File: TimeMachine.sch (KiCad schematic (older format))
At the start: 52 parts, among them J1 AppleIIBus, J2 JTAG, U1 EPM7128SL84, U2 DS1215, U3 74AHCT04, U4 AS6C8008, U5 39F040, Y1 32k768

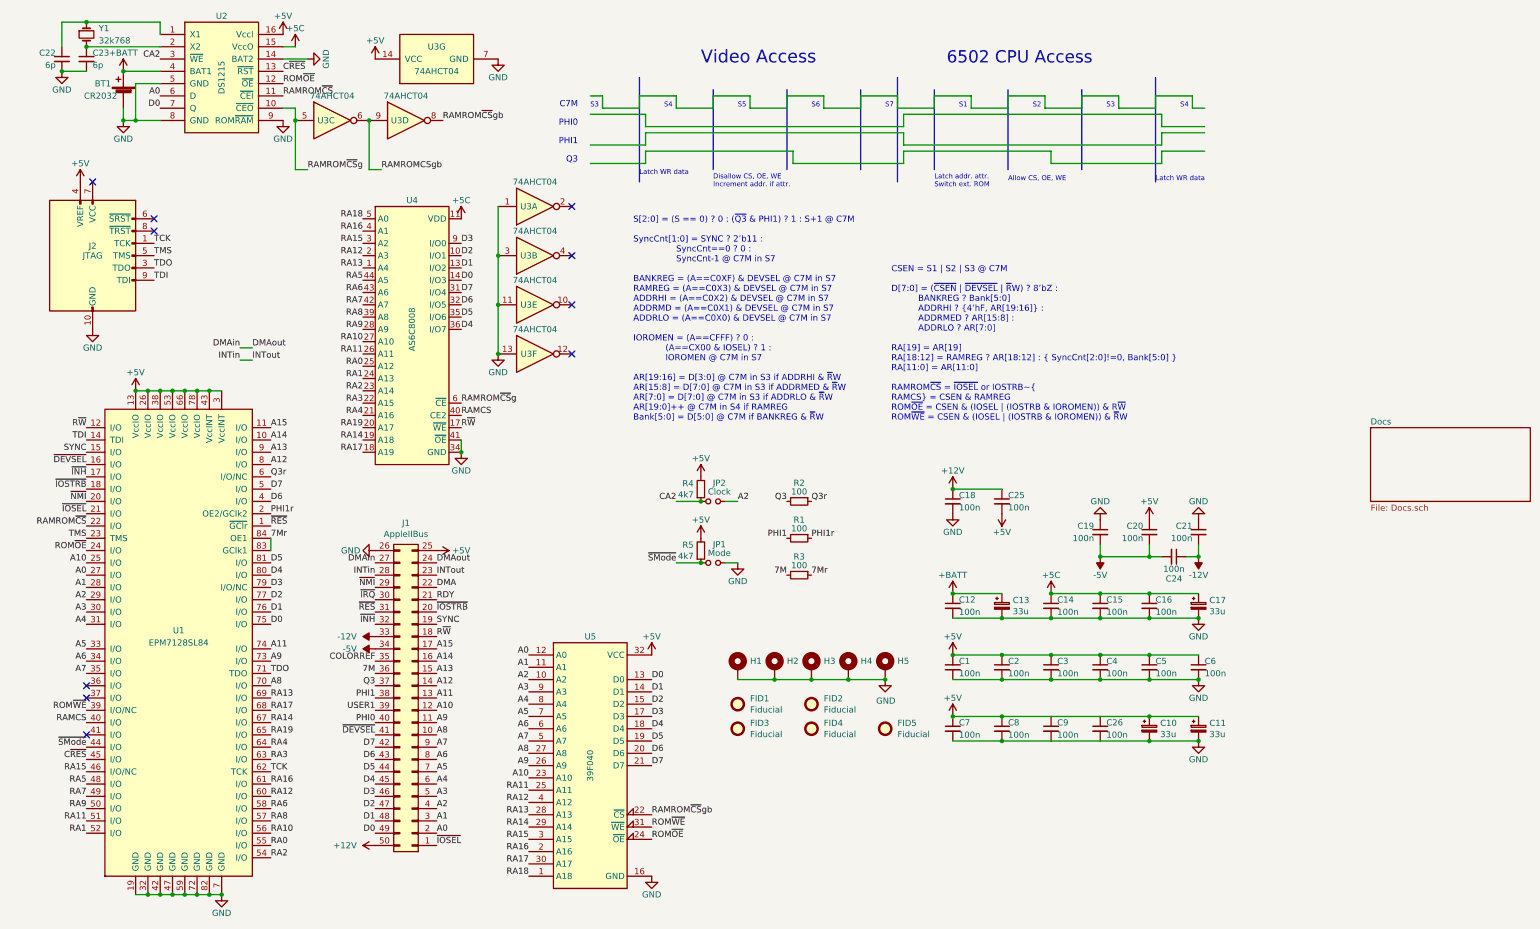
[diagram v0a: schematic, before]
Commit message: Buffered data bus with CPLD
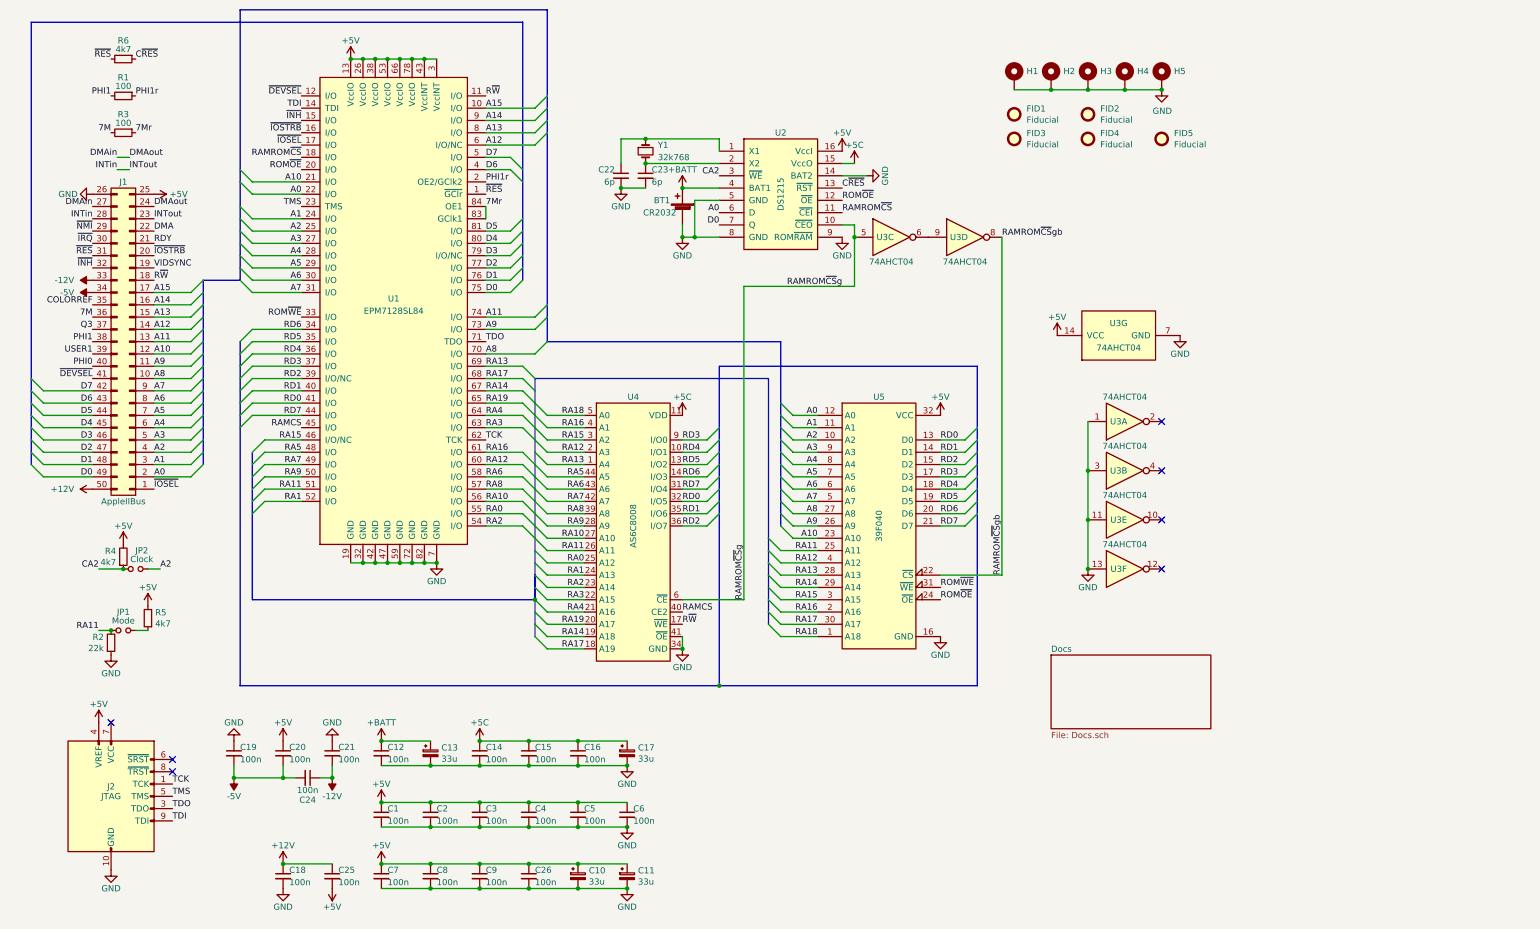
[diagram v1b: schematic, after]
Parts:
- added R6: 4k7, stdpads:R_0805, symbol Device:R_Small
- R2: value 100 -> 22k
- U3: footprint Package_SO:SOIC-14_3.9x8.7mm_P1.27mm -> stdpads:SOIC-14_3.9mm
- U3: footprint 74AHCT04 -> stdpads:SOIC-14_3.9mm
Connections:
- net labels added: RD0, RD1, RD2, RD3, RD4, RD5, RD6, RD7, VIDSYNC
- net labels removed: Q3r, RAMROMCSgb, SYNC, ~SMode~
- wire segments 145 -> 217
- no-connect marks 10 -> 7
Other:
- note removed: "6502 CPU Access"
- note removed: "Allow CS, OE, WE"
- note removed: "C7M"
- note removed: "CSEN = S1 | S2 | S3 @ C7M\n\nD[7:0] = (~CSEN~ | ~DEVSEL~ | ~R~W) ? 8’bZ :\n BANKREG ? Bank[5:0]\n ADDRHI ? {4’hF, AR[19:16]} : \n ADDRMED ? AR[15:8] : \n ADDRLO ? AR[7:0]\n\nRA[19] = AR[19]\nRA[18:12] = RAMREG ? AR[18:12] : { SyncCnt[2:0]!=0, Bank[5:0] }\nRA[11:0] = AR[11:0]\n\nRAMROM~CS~ = ~IOSEL or IOSTRB~\nRAMCS = CSEN & RAMREG\nROM~OE~ = CSEN & (IOSEL | (IOSTRB & IOROMEN)) & R~W~\nROM~WE~ = C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"
- note removed: "Disallow CS, OE, WE\nIncrement addr. if attr."
- note removed: "Latch WR data"
- note removed: "Latch addr. attr.\nSwitch ext. ROM"
- note removed: "PHI0"
- note removed: "PHI1"
- note removed: "Q3"
- note removed: "S1"
- note removed: "S2"
- note removed: "S3"
- note removed: "S4"
- note removed: "S5"
- note removed: "S6"
- note removed: "S7"
- note removed: "S[2:0] = (S == 0) ? 0 : (~Q3~ & PHI1) ? 1 : S+1 @ C7M\n\nSyncCnt[1:0] = SYNC ? 2’b11 : \n SyncCnt==0 ? 0 :\n SyncCnt-1 @ C7M in S7\n\nBANKREG = (A==C0XF) & DEVSEL @ C7M in S7\nRAMREG = (A==C0X3) & DEVSEL @ C7M in S7\nADDRHI = (A==C0X2) & DEVSEL @ C7M in S7\nADDRMD = (A==C0X1) & DEVSEL @ C7M in S7\nADDRLO = (A==C0X0) & DEVSEL @ C7M in S7\n\nIOROMEN = (A==CFFF) ? 0 :\n (A==CX00 & IOSEL) ? 1 :\n IOR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"
- note removed: "Video Access"
- moved on the sheet: BT1, C1, C10, C11, C12, C13, C14, C15, C16, C17, C18, C19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

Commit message: Changed ROM OE strategy
Has gerbers submitted to JLCPCB though
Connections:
- net GND: now also U3.9; no longer U3.3
- net RAMROM~CS~: now also U1.20 (I/O); no longer U1.18 (I/O)
- net R~W~: now also U3.3, U5.31 (~WE~)
- net ~IOSEL~: now also U1.18 (I/O); no longer U1.17 (I/O)
- net ~OE~: now reaches U3.4
- net ~OE~: now also U2.12 (~OE~), U5.24 (~OE~)
- net RAMROMCSgb: now reaches U3.6
- net RAMROMCSgb: now also U1.33 (I/O); no longer U3.9
- net RAMROM~CS~gb: no longer names the net of U3.8
- net RAMROM~CS~gb: no longer U5.22 (~CS~)
- removed net ROM~OE~: U1.20 (I/O), U2.12 (~OE~), U5.24 (~OE~)
- removed net ROM~WE~: U1.33 (I/O), U5.31 (~WE~)
- new net ROM~CS~: U1.17 (I/O), U5.22 (~CS~)
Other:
- moved on the sheet: U3A, U3B, U3E, U3F, U3G
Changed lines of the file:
@@
 Wire Wire Line
 	4300 2300 4300 2200
-Text Label 2800 1800 2    50   ~ 0
+Text Label 2800 1900 2    50   ~ 0
 RAMROM~CS~
-Text Label 2800 3100 2    50   ~ 0
-ROM~WE~
 Wire Wire Line
 	3200 5100 3300 5100
@@
 Text Label 2800 1500 2    50   ~ 0
 ~INH~
-Text Label 2800 1700 2    50   ~ 0
+Text Label 2800 1800 2    50   ~ 0
 ~IOSEL~
 Text Label 4300 1300 0    50   ~ 0
@@
 $EndComp
 Text Label 8500 2450 0    50   ~ 0
-RAMROM~CS~gb
+RAMROMCSgb
 Text Label 4300 2800 0    50   ~ 0
 D1
@@
 ~IOSEL~
 Text Label 8000 5400 0    50   ~ 0
-ROM~OE~
-Text Label 2800 1900 2    50   ~ 0
-ROM~OE~
+~OE~
 $Comp
 L Device:C_Small C21
@@
 	1    0    0    -1
 $EndComp
-Text Label 8000 5300 0    50   ~ 0
-ROM~WE~
 Text Label 4300 1400 0    50   ~ 0
 A15
@@
 	6400 5400 6400 2850
 Wire Wire Line
-	8500 2450 8500 5200
-Wire Wire Line
 	7300 2450 7300 2850
 Text Label 7200 2850 2    50   ~ 0
@@
 Text Label 7200 2050 0    50   ~ 0
 C~RES~
-$Comp
-L 74xx:74HC04 U3
-U 4 1 5E7FE38F
-P 8200 2450
-F 0 "U3" H 8150 2450 50  0000 C CNN
-F 1 "74AHCT04" H 8200 2250 50  0000 C CNN
-F 2 "stdpads:SOIC-14_3.9mm" H 8200 2450 50  0001 C CNN
-F 3 "https://assets.nexperia.com/documents/data-sheet/74HC_HCT04.pdf" H 8200 2450 50  0001 C CNN
-	4    8200 2450
-	1    0    0    -1
-$EndComp
-Text Label 7200 2150 0    50   ~ 0
-ROM~OE~
 $Comp
 L power:GND #PWR0123
@@
 Wire Wire Line
 	5900 5400 6400 5400
-Wire Wire Line
-	8000 5200 8500 5200
-Text Label 8500 5200 1    50   ~ 0
-RAMROM~CS~gb
-$Comp
-L 74xx:74HC04 U3
-U 1 1 5E4D40B3
-P 9500 3950
-AR Path="/5E4D40B3" Ref="U3"  Part="1"
-AR Path="/5D3B15F6/5E4D40B3" Ref="U?"  Part="1"
-F 0 "U3" H 9450 3950 50  0000 C CNN
-F 1 "74AHCT04" H 9500 3750 50  0000 C CNN
-F 2 "stdpads:SOIC-14_3.9mm" H 9500 3950 50  0001 C CNN
-F 3 "https://assets.nexperia.com/documents/data-sheet/74HC_HCT04.pdf" H 9500 3950 50  0001 C CNN
-	1    9500 3950
-	1    0    0    1
-$EndComp
-$Comp
-L 74xx:74HC04 U3
-U 2 1 5E4D40B9
-P 9500 4350
-AR Path="/5E4D40B9" Ref="U3"  Part="2"
-AR Path="/5D3B15F6/5E4D40B9" Ref="U?"  Part="2"
-F 0 "U3" H 9450 4350 50  0000 C CNN
-F 1 "74AHCT04" H 9500 4150 50  0000 C CNN
-F 2 "stdpads:SOIC-14_3.9mm" H 9500 4350 50  0001 C CNN
-F 3 "https://assets.nexperia.com/documents/data-sheet/74HC_HCT04.pdf" H 9500 4350 50  0001 C CNN
-	2    9500 4350
-	1    0    0    1
-$EndComp
+Text Label 8000 5200 0    50   ~ 0
+ROM~CS~
 $Comp
 L 74xx:74HC04 U3
 U 7 1 5E4D40BF
-P 9450 3250
+P 9450 3050
 AR Path="/5E4D40BF" Ref="U3"  Part="7"
 AR Path="/5D3B15F6/5E4D40BF" Ref="U?"  Part="7"
-F 0 "U3" V 9550 3250 50  0000 C CNN
-F 1 "74AHCT04" V 9350 3250 50  0000 C CNN
-F 2 "stdpads:SOIC-14_3.9mm" H 9450 3250 50  0001 C CNN
-F 3 "https://assets.nexperia.com/documents/data-sheet/74HC_HCT04.pdf" H 9450 3250 50  0001 C CNN
-	7    9450 3250
+F 0 "U3" V 9550 3050 50  0000 C CNN
+F 1 "74AHCT04" V 9350 3050 50  0000 C CNN
+F 2 "stdpads:SOIC-14_3.9mm" H 9450 3050 50  0001 C CNN
+F 3 "https://assets.nexperia.com/documents/data-sheet/74HC_HCT04.pdf" H 9450 3050 50  0001 C CNN
+	7    9450 3050
 	0    -1   -1   0
 $EndComp
@@
 L power:+5V #PWR0125
 U 1 1 5E4D40C5
-P 8950 3250
+P 8950 3050
 AR Path="/5E4D40C5" Ref="#PWR0125"  Part="1"
 AR Path="/5D3B15F6/5E4D40C5" Ref="#PWR?"  Part="1"
-F 0 "#PWR0125" H 8950 3100 50  0001 C CNN
-F 1 "+5V" H 8950 3400 50  0000 C CNN
-F 2 "" H 8950 3250 50  0001 C CNN
-F 3 "" H 8950 3250 50  0001 C CNN
-	1    8950 3250
+F 0 "#PWR0125" H 8950 2900 50  0001 C CNN
+F 1 "+5V" H 8950 3200 50  0000 C CNN
+F 2 "" H 8950 3050 50  0001 C CNN
+F 3 "" H 8950 3050 50  0001 C CNN
+	1    8950 3050
 	1    0    0    -1
 $EndComp
@@
 L power:GND #PWR0126
 U 1 1 5E4D40CB
-P 9950 3250
+P 9950 3050
 AR Path="/5E4D40CB" Ref="#PWR0126"  Part="1"
 AR Path="/5D3B15F6/5E4D40CB" Ref="#PWR?"  Part="1"
-F 0 "#PWR0126" H 9950 3000 50  0001 C CNN
-F 1 "GND" H 9950 3100 50  0000 C CNN
-F 2 "" H 9950 3250 50  0001 C CNN
-F 3 "" H 9950 3250 50  0001 C CNN
-	1    9950 3250
-	1    0    0    -1
-$EndComp
-NoConn ~ 9800 5150
-NoConn ~ 9800 4750
-NoConn ~ 9800 4350
-NoConn ~ 9800 3950
+F 0 "#PWR0126" H 9950 2800 50  0001 C CNN
+F 1 "GND" H 9950 2900 50  0000 C CNN
+F 2 "" H 9950 3050 50  0001 C CNN
+F 3 "" H 9950 3050 50  0001 C CNN
+	1    9950 3050
+	1    0    0    -1
+$EndComp
+NoConn ~ 9800 5450
+NoConn ~ 9800 5050
+NoConn ~ 9800 4250
 $Comp
 L 74xx:74HC04 U3
 U 6 1 5E4D40D5
-P 9500 5150
+P 9500 5450
 AR Path="/5E4D40D5" Ref="U3"  Part="6"
 AR Path="/5D3B15F6/5E4D40D5" Ref="U?"  Part="6"
-F 0 "U3" H 9450 5150 50  0000 C CNN
-F 1 "74AHCT04" H 9500 5350 50  0000 C CNN
-F 2 "stdpads:SOIC-14_3.9mm" H 9500 5150 50  0001 C CNN
-F 3 "https://assets.nexperia.com/documents/data-sheet/74HC_HCT04.pdf" H 9500 5150 50  0001 C CNN
-	6    9500 5150
-	1    0    0    -1
-$EndComp
-Wire Wire Line
-	9200 5150 9200 4750
-Connection ~ 9200 4750
+F 0 "U3" H 9450 5450 50  0000 C CNN
+F 1 "74AHCT04" H 9500 5650 50  0000 C CNN
+F 2 "stdpads:SOIC-14_3.9mm" H 9500 5450 50  0001 C CNN
+F 3 "https://assets.nexperia.com/documents/data-sheet/74HC_HCT04.pdf" H 9500 5450 50  0001 C CNN
+	6    9500 5450
+	1    0    0    -1
+$EndComp
+Wire Wire Line
+	9200 5450 9200 5050
+Connection ~ 9200 5050
 $Comp
 L 74xx:74HC04 U3
 U 5 1 5E4D40DD
-P 9500 4750
+P 9500 5050
 AR Path="/5E4D40DD" Ref="U3"  Part="5"
 AR Path="/5D3B15F6/5E4D40DD" Ref="U?"  Part="5"
-F 0 "U3" H 9450 4750 50  0000 C CNN
-F 1 "74AHCT04" H 9500 4950 50  0000 C CNN
-F 2 "stdpads:SOIC-14_3.9mm" H 9500 4750 50  0001 C CNN
-F 3 "https://assets.nexperia.com/documents/data-sheet/74HC_HCT04.pdf" H 9500 4750 50  0001 C CNN
-	5    9500 4750
-	1    0    0    -1
-$EndComp
-Wire Wire Line
-	9200 3950 9200 4350
-Connection ~ 9200 4350
-Wire Wire Line
-	9200 4350 9200 4750
+F 0 "U3" H 9450 5050 50  0000 C CNN
+F 1 "74AHCT04" H 9500 5250 50  0000 C CNN
+F 2 "stdpads:SOIC-14_3.9mm" H 9500 5050 50  0001 C CNN
+F 3 "https://assets.nexperia.com/documents/data-sheet/74HC_HCT04.pdf" H 9500 5050 50  0001 C CNN
+	5    9500 5050
+	1    0    0    -1
+$EndComp
+Wire Wire Line
+	9200 4650 9200 5050
 $Comp
 L power:GND #PWR0130
 U 1 1 5E4D40E6
-P 9200 5150
+P 9200 5450
 AR Path="/5E4D40E6" Ref="#PWR0130"  Part="1"
 AR Path="/5D3B15F6/5E4D40E6" Ref="#PWR?"  Part="1"
-F 0 "#PWR0130" H 9200 4900 50  0001 C CNN
-F 1 "GND" H 9200 5000 50  0000 C CNN
-F 2 "" H 9200 5150 50  0001 C CNN
-F 3 "" H 9200 5150 50  0001 C CNN
-	1    9200 5150
-	1    0    0    -1
-$EndComp
-Connection ~ 9200 5150
+F 0 "#PWR0130" H 9200 5200 50  0001 C CNN
+F 1 "GND" H 9200 5300 50  0000 C CNN
+F 2 "" H 9200 5450 50  0001 C CNN
+F 3 "" H 9200 5450 50  0001 C CNN
+	1    9200 5450
+	1    0    0    -1
+$EndComp
+Connection ~ 9200 5450
 Wire Bus Line
 	2300 600  4800 600
@@
 	1    0    0    -1
 $EndComp
+Text Label 9800 3850 0    50   ~ 0
+~OE~
+Text Label 7200 2150 0    50   ~ 0
+~OE~
+Text Label 9200 3850 2    50   ~ 0
+R~W~
+Text Label 8000 5300 0    50   ~ 0
+R~W~
+Wire Wire Line
+	7900 2450 8500 2450
+Text Label 2800 3100 2    50   ~ 0
+RAMROMCSgb
+Text Label 2800 1700 2    50   ~ 0
+ROM~CS~
+$Comp
+L 74xx:74HC04 U3
+U 4 1 5D5119EB
+P 9500 4650
+F 0 "U3" H 9450 4650 50  0000 C CNN
+F 1 "74AHCT04" H 9500 4450 50  0000 C CNN
+F 2 "stdpads:SOIC-14_3.9mm" H 9500 4650 50  0001 C CNN
+F 3 "https://assets.nexperia.com/documents/data-sheet/74HC_HCT04.pdf" H 9500 4650 50  0001 C CNN
+	4    9500 4650
+	1    0    0    1
+$EndComp
+$Comp
+L 74xx:74HC04 U3
+U 2 1 5E4D40B9
+P 9500 3850
+AR Path="/5E4D40B9" Ref="U3"  Part="2"
+AR Path="/5D3B15F6/5E4D40B9" Ref="U?"  Part="2"
+F 0 "U3" H 9450 3850 50  0000 C CNN
+F 1 "74AHCT04" H 9500 3650 50  0000 C CNN
+F 2 "stdpads:SOIC-14_3.9mm" H 9500 3850 50  0001 C CNN
+F 3 "https://assets.nexperia.com/documents/data-sheet/74HC_HCT04.pdf" H 9500 3850 50  0001 C CNN
+	2    9500 3850
+	1    0    0    1
+$EndComp
+$Comp
+L 74xx:74HC04 U3
+U 1 1 5E4D40B3
+P 9500 4250
+AR Path="/5E4D40B3" Ref="U3"  Part="1"
+AR Path="/5D3B15F6/5E4D40B3" Ref="U?"  Part="1"
+F 0 "U3" H 9450 4250 50  0000 C CNN
+F 1 "74AHCT04" H 9500 4050 50  0000 C CNN
+F 2 "stdpads:SOIC-14_3.9mm" H 9500 4250 50  0001 C CNN
+F 3 "https://assets.nexperia.com/documents/data-sheet/74HC_HCT04.pdf" H 9500 4250 50  0001 C CNN
+	1    9500 4250
+	1    0    0    1
+$EndComp
+Wire Wire Line
+	9200 4250 9200 4650
+Connection ~ 9200 4650
+NoConn ~ 9800 4650
 Wire Bus Line
 	4700 5200 4700 5400

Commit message: Can't fit...
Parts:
- removed C22, C23: 6p, stdpads:C_0805, symbol Device:C_Small
- Y1: footprint stdpads:Crystal_HC49-SMD -> Crystal_C26-LF_D2.1mm_L6.5mm_Horizontal_1EP_style1
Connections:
- net RA18: now also U1.15 (I/O)
- net ~INH~: no longer U1.15 (I/O)
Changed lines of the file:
@@
 	3800 5100 3900 5100
 Connection ~ 3900 5100
-Text Label 2800 1500 2    50   ~ 0
-~INH~
 Text Label 2800 1800 2    50   ~ 0
 ~IOSEL~
@@
 	4700 4100 4600 4000
 Wire Bus Line
-	2400 5400 4700 5400
+	2400 5700 4700 5700
 Entry Wire Line
 	6200 4300 6100 4400
@@
 Entry Wire Line
 	4700 3800 4800 3900
-Connection ~ 4700 5400
 Wire Bus Line
 	2300 6100 6200 6100
@@
 Wire Wire Line
 	6200 1650 6200 1750
-Connection ~ 5600 1650
-Wire Wire Line
-	5400 1650 5400 1850
-Wire Wire Line
-	5600 1650 5400 1650
-Connection ~ 5400 2050
-Wire Wire Line
-	5600 2050 5400 2050
 Wire Wire Line
 	5600 1650 6200 1650
 Wire Wire Line
 	5600 1850 6200 1850
-$Comp
-L power:GND #PWR0104
-U 1 1 5D553337
-P 5400 2050
-F 0 "#PWR0104" H 5400 1800 50  0001 C CNN
-F 1 "GND" H 5400 1900 50  0000 C CNN
-F 2 "" H 5400 2050 50  0001 C CNN
-F 3 "" H 5400 2050 50  0001 C CNN
-	1    5400 2050
-	1    0    0    -1
-$EndComp
-$Comp
-L Device:C_Small C22
-U 1 1 5D552FB7
-P 5400 1950
-F 0 "C22" H 5450 2000 50  0000 L CNN
-F 1 "6p" H 5450 1900 50  0000 L CNN
-F 2 "stdpads:C_0805" H 5400 1950 50  0001 C CNN
-F 3 "~" H 5400 1950 50  0001 C CNN
-	1    5400 1950
-	-1   0    0    -1
-$EndComp
-$Comp
-L Device:C_Small C23
-U 1 1 5D551238
-P 5600 1950
-F 0 "C23" H 5650 2000 50  0000 L CNN
-F 1 "6p" H 5650 1900 50  0000 L CNN
-F 2 "stdpads:C_0805" H 5600 1950 50  0001 C CNN
-F 3 "~" H 5600 1950 50  0001 C CNN
-	1    5600 1950
-	1    0    0    -1
-$EndComp
 $Comp
 L Device:Crystal_Small Y1
@@
 F 0 "Y1" V 5550 1850 50  0000 L CNN
 F 1 "32k768" V 5650 1850 50  0000 L CNN
-F 2 "stdpads:Crystal_HC49-SMD" H 5600 1750 50  0001 C CNN
+F 2 "Crystal_C26-LF_D2.1mm_L6.5mm_Horizontal_1EP_style1" H 5600 1750 50  0001 C CNN
 F 3 "~" H 5600 1750 50  0001 C CNN
 	1    5600 1750
 	0    1    1    0
 $EndComp
-Connection ~ 5600 1850
 Text Label 6200 2250 2    50   ~ 0
 A0
@@
 Connection ~ 9200 4650
 NoConn ~ 9800 4650
-Wire Bus Line
-	4700 5200 4700 5400
-Wire Bus Line
-	4700 5400 4700 5700
+Text Label 2800 1500 2    50   ~ 0
+RA18
+Wire Wire Line
+	2800 1500 2200 1500
+Entry Wire Line
+	2100 1600 2200 1500
+Wire Bus Line
+	2100 1600 2100 4200
+Wire Bus Line
+	2100 4200 2400 4200
 Wire Bus Line
 	2300 600  2300 2800
 Wire Bus Line
-	2400 4200 2400 5400
+	2400 4200 2400 5700
 Wire Bus Line
 	4800 600  4800 3300
@@
 	2000 2800 2000 4300
 Wire Bus Line
-	4700 3600 4700 5400
+	4700 3600 4700 5700
 $EndSCHEMATC

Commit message: Merged changes from GR8RAM, e.g. pipelined add
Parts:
- Y1: symbol Device:Crystal_Small -> Device:Crystal_GND3_Small
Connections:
- net 7Mr: no longer U1.84 (OE1)
- net A12: now also U1.84 (OE1); no longer U1.6 (I/O/NC)
- net A13: now also U1.6 (I/O/NC); no longer U1.8 (I/O)
- net A14: now also U1.8 (I/O); no longer U1.9 (I/O)
- net A15: now also U1.9 (I/O); no longer U1.10 (I/O)
- net GND: now also Y1.3
- net RA18: now also U1.12 (I/O); no longer U1.15 (I/O)
- net R~W~: now also U1.10 (I/O); no longer U1.11 (I/O)
- net ~DEVSEL~: now also U1.11 (I/O); no longer U1.12 (I/O)
- net ~INH~: now also U1.15 (I/O)
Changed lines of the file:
@@
 Text Label 4300 3600 0    50   ~ 0
 RA17
-Text Label 4300 2200 0    50   ~ 0
+Text Label 4300 2300 0    50   ~ 0
 7Mr
-Wire Wire Line
-	4300 2300 4300 2200
 Text Label 2800 1900 2    50   ~ 0
 RAMROM~CS~
@@
 Text Label 2800 1800 2    50   ~ 0
 ~IOSEL~
+Text Label 4300 1400 0    50   ~ 0
+R~W~
 Text Label 4300 1300 0    50   ~ 0
-R~W~
-Text Label 2800 1300 2    50   ~ 0
 ~DEVSEL~
 Text Label 2800 2100 2    50   ~ 0
@@
 	1    0    0    -1
 $EndComp
-Text Label 4300 1400 0    50   ~ 0
+Text Label 4300 1500 0    50   ~ 0
 A15
-Text Label 4300 1500 0    50   ~ 0
+Text Label 4300 1600 0    50   ~ 0
 A14
-Text Label 4300 1600 0    50   ~ 0
+Text Label 4300 1700 0    50   ~ 0
 A13
-Text Label 4300 1700 0    50   ~ 0
+Text Label 4300 2200 0    50   ~ 0
 A12
 Text Label 4300 2900 0    50   ~ 0
@@
 	2300 2800 2400 2900
 Entry Wire Line
-	4800 1300 4700 1400
-Entry Wire Line
 	4800 1400 4700 1500
 Entry Wire Line
@@
 Entry Wire Line
 	4800 1600 4700 1700
+Entry Wire Line
+	4800 2100 4700 2200
 Entry Wire Line
 	4600 2000 4500 1900
@@
 	4300 2900 4500 2900
 Wire Wire Line
-	4300 1400 4700 1400
-Wire Wire Line
 	4300 1500 4700 1500
 Wire Wire Line
 	4300 1600 4700 1600
 Wire Wire Line
+	4300 1700 4700 1700
+Wire Wire Line
 	4300 1800 4500 1800
 Wire Wire Line
 	4300 1900 4500 1900
 Wire Wire Line
-	4300 1700 4700 1700
+	4300 2200 4700 2200
 Wire Bus Line
 	600  700  4600 700
@@
 	5600 1850 6200 1850
 $Comp
-L Device:Crystal_Small Y1
+L Device:Crystal_GND3_Small Y1
 U 1 1 5D320127
 P 5600 1750
@@
 Connection ~ 9200 4650
 NoConn ~ 9800 4650
+Text Label 2800 1300 2    50   ~ 0
+RA18
+Entry Wire Line
+	2100 1400 2200 1300
+Wire Bus Line
+	2100 4200 2400 4200
+Wire Wire Line
+	2200 1300 2800 1300
+Wire Bus Line
+	2100 1400 2100 4200
 Text Label 2800 1500 2    50   ~ 0
-RA18
-Wire Wire Line
-	2800 1500 2200 1500
-Entry Wire Line
-	2100 1600 2200 1500
-Wire Bus Line
-	2100 1600 2100 4200
-Wire Bus Line
-	2100 4200 2400 4200
+~INH~
 Wire Bus Line
 	2300 600  2300 2800
@@
 Wire Bus Line
 	4700 3600 4700 5700
+$Comp
+L power:GND #PWR?
+U 1 1 5D855455
+P 5500 1750
+F 0 "#PWR?" H 5500 1500 50  0001 C CNN
+F 1 "GND" H 5505 1577 50  0000 C CNN
+F 2 "" H 5500 1750 50  0001 C CNN
+F 3 "" H 5500 1750 50  0001 C CNN
+	1    5500 1750
+	1    0    0    -1
+$EndComp
 $EndSCHEMATC
